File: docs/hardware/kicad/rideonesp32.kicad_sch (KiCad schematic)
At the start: 0 parts

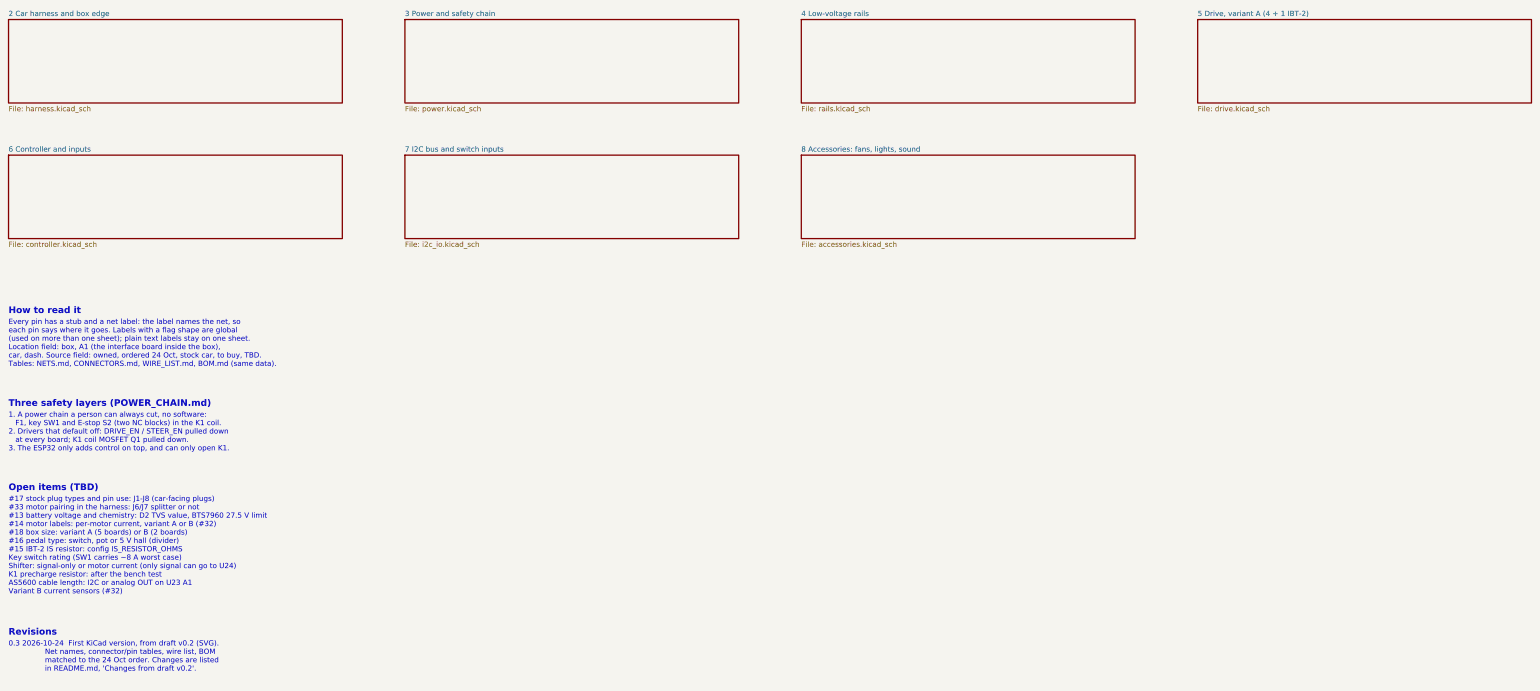
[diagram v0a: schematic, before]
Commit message: Schematic index: say what each sheet box holds and how to open it
The sheet symbols on page 1 were empty boxes, which read as missing
content. Each now carries a short summary of its sheet.

Co-Authored-By: Claude Opus 5.5 (1M context) <noreply@anthropic.com>
Claude-Session: https://claude.ai/code/session_01BSRw381bu7GTvawcDjL4S1
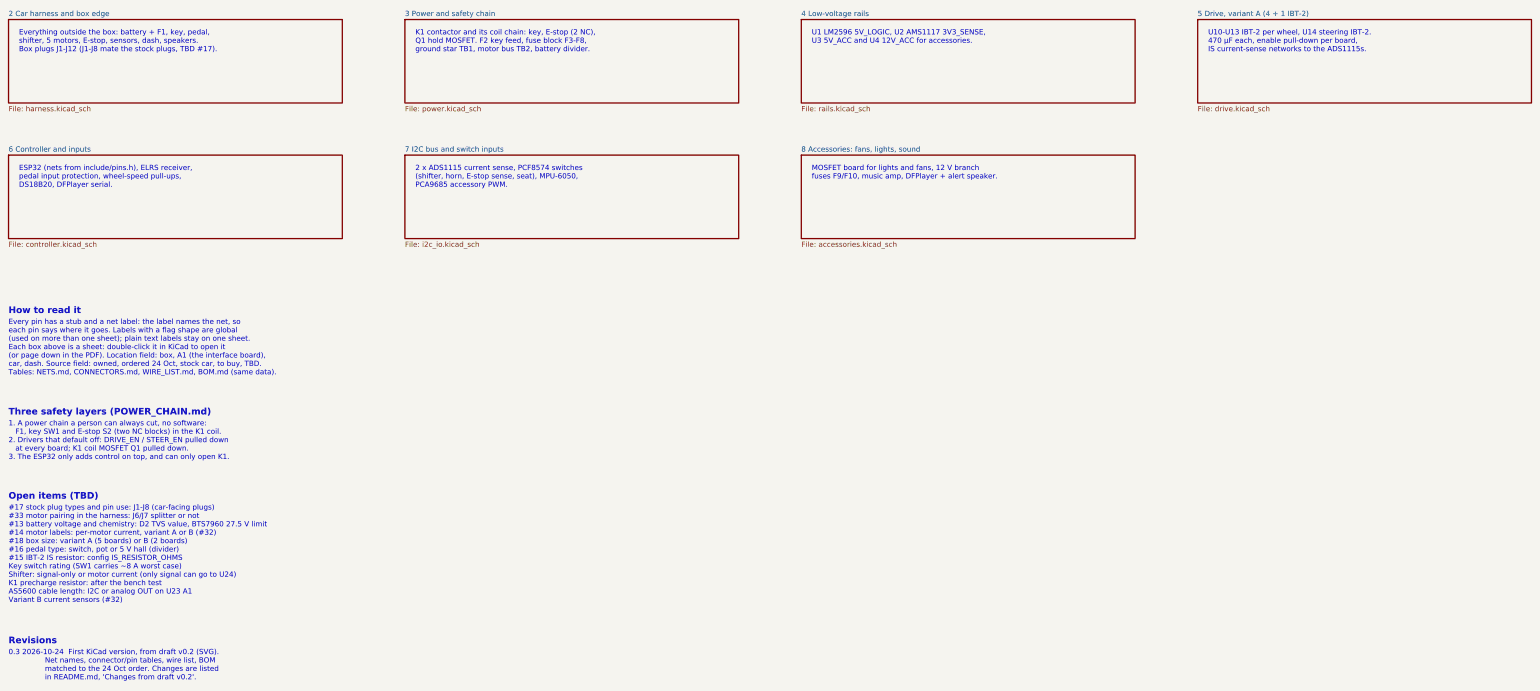
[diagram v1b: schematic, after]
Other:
- note added: "2 x ADS1115 current sense, PCF8574 switches (shifter, horn, E-stop sense, seat), MPU-6050, PCA9685 accessory PWM."
- note added: "ESP32 (nets from include/pins.h), ELRS receiver, pedal input protection, wheel-speed pull-ups, DS18B20, DFPlayer serial."
- note added: "Every pin has a stub and a net label: the label names the net, so each pin says where it goes. Labels with a flag shape are global (used on more than one sheet); plain text labels stay on one sheet. Each box above is a sheet: double-click it in KiCad to open it (or page down in the PDF). Location field: box, A1 (the interface board), car, dash. Source field: owned, ordered 24 Oct, stock car, to b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"
- note added: "Everything outside the box: battery + F1, key, pedal, shifter, 5 motors, E-stop, sensors, dash, speakers. Box plugs J1-J12 (J1-J8 mate the stock plugs, TBD #17)."
- note added: "K1 contactor and its coil chain: key, E-stop (2 NC), Q1 hold MOSFET. F2 key feed, fuse block F3-F8, ground star TB1, motor bus TB2, battery divider."
- note added: "MOSFET board for lights and fans, 12 V branch fuses F9/F10, music amp, DFPlayer + alert speaker."
- note added: "U1 LM2596 5V_LOGIC, U2 AMS1117 3V3_SENSE, U3 5V_ACC and U4 12V_ACC for accessories."
- note added: "U10-U13 IBT-2 per wheel, U14 steering IBT-2. 470 µF each, enable pull-down per board, IS current-sense networks to the ADS1115s."
- note removed: "Every pin has a stub and a net label: the label names the net, so each pin says where it goes. Labels with a flag shape are global (used on more than one sheet); plain text labels stay on one sheet. Location field: box, A1 (the interface board inside the box), car, dash. Source field: owned, ordered 24 Oct, stock car, to buy, TBD. Tables: NETS.md, CONNECTORS.md, WIRE_LIST.md, BOM.md (same data)."
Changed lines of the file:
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@@
   (instances (project "rideonesp32" (path "/e0e78d72-bf5c-51da-8e0f-d8642949b63b" (page "2"))))
 )
+(text "Everything outside the box: battery + F1, key, pedal,\nshifter, 5 motors, E-stop, sensors, dash, speakers.\nBox plugs J1-J12 (J1-J8 mate the stock plugs, TBD #17)." (exclude_from_sim no) (at 22.86 33.02 0) (effects (font (size 1.27 1.27)) (justify left top)))
 (sheet (at 116.84 30.48) (size 81.28 20.32) (exclude_from_sim no) (in_bom yes) (on_board yes) (dnp no)
   (stroke (width 0.1524) (type solid)) (fill (color 0 0 0 0.0000))
@@
   (instances (project "rideonesp32" (path "/e0e78d72-bf5c-51da-8e0f-d8642949b63b" (page "3"))))
 )
+(text "K1 contactor and its coil chain: key, E-stop (2 NC),\nQ1 hold MOSFET. F2 key feed, fuse block F3-F8,\nground star TB1, motor bus TB2, battery divider." (exclude_from_sim no) (at 119.38 33.02 0) (effects (font (size 1.27 1.27)) (justify left top)))
 (sheet (at 213.36 30.48) (size 81.28 20.32) (exclude_from_sim no) (in_bom yes) (on_board yes) (dnp no)
   (stroke (width 0.1524) (type solid)) (fill (color 0 0 0 0.0000))
@@
   (instances (project "rideonesp32" (path "/e0e78d72-bf5c-51da-8e0f-d8642949b63b" (page "4"))))
 )
+(text "U1 LM2596 5V_LOGIC, U2 AMS1117 3V3_SENSE,\nU3 5V_ACC and U4 12V_ACC for accessories." (exclude_from_sim no) (at 215.9 33.02 0) (effects (font (size 1.27 1.27)) (justify left top)))
 (sheet (at 309.88 30.48) (size 81.28 20.32) (exclude_from_sim no) (in_bom yes) (on_board yes) (dnp no)
   (stroke (width 0.1524) (type solid)) (fill (color 0 0 0 0.0000))
@@
   (instances (project "rideonesp32" (path "/e0e78d72-bf5c-51da-8e0f-d8642949b63b" (page "5"))))
 )
+(text "U10-U13 IBT-2 per wheel, U14 steering IBT-2.\n470 µF each, enable pull-down per board,\nIS current-sense networks to the ADS1115s." (exclude_from_sim no) (at 312.42 33.02 0) (effects (font (size 1.27 1.27)) (justify left top)))
 (sheet (at 20.32 63.5) (size 81.28 20.32) (exclude_from_sim no) (in_bom yes) (on_board yes) (dnp no)
   (stroke (width 0.1524) (type solid)) (fill (color 0 0 0 0.0000))
@@
   (instances (project "rideonesp32" (path "/e0e78d72-bf5c-51da-8e0f-d8642949b63b" (page "6"))))
 )
+(text "ESP32 (nets from include/pins.h), ELRS receiver,\npedal input protection, wheel-speed pull-ups,\nDS18B20, DFPlayer serial." (exclude_from_sim no) (at 22.86 66.04 0) (effects (font (size 1.27 1.27)) (justify left top)))
 (sheet (at 116.84 63.5) (size 81.28 20.32) (exclude_from_sim no) (in_bom yes) (on_board yes) (dnp no)
   (stroke (width 0.1524) (type solid)) (fill (color 0 0 0 0.0000))
@@
   (instances (project "rideonesp32" (path "/e0e78d72-bf5c-51da-8e0f-d8642949b63b" (page "7"))))
 )
+(text "2 x ADS1115 current sense, PCF8574 switches\n(shifter, horn, E-stop sense, seat), MPU-6050,\nPCA9685 accessory PWM." (exclude_from_sim no) (at 119.38 66.04 0) (effects (font (size 1.27 1.27)) (justify left top)))
 (sheet (at 213.36 63.5) (size 81.28 20.32) (exclude_from_sim no) (in_bom yes) (on_board yes) (dnp no)
   (stroke (width 0.1524) (type solid)) (fill (color 0 0 0 0.0000))
@@
   (instances (project "rideonesp32" (path "/e0e78d72-bf5c-51da-8e0f-d8642949b63b" (page "8"))))
 )
+(text "MOSFET board for lights and fans, 12 V branch\nfuses F9/F10, music amp, DFPlayer + alert speaker." (exclude_from_sim no) (at 215.9 66.04 0) (effects (font (size 1.27 1.27)) (justify left top)))
 (text "How to read it" (exclude_from_sim no) (at 20.32 100.52 0) (effects (font (size 1.6 1.6) (bold yes)) (justify left top)))
-(text "Every pin has a stub and a net label: the label names the net, so\neach pin says where it goes. Labels with a flag shape are global\n(used on more than one sheet); plain text labels stay on one sheet.\nLocation field: box, A1 (the interface board inside the box),\ncar, dash. Source field: owned, ordered 24 Oct, stock car, to buy, TBD.\nTables: NETS.md, CONNECTORS.md, WIRE_LIST.md, BOM.md (same data)." (exclude_from_sim no) (at 20.32 103.52 0) (effects (font (size 1.27 1.27)) (justify left top)))
-(text "Three safety layers (POWER_CHAIN.md)" (exclude_from_sim no) (at 20.32 123.12 0) (effects (font (size 1.6 1.6) (bold yes)) (justify left top)))
-(text "1. A power chain a person can always cut, no software:\n   F1, key SW1 and E-stop S2 (two NC blocks) in the K1 coil.\n2. Drivers that default off: DRIVE_EN / STEER_EN pulled down\n   at every board; K1 coil MOSFET Q1 pulled down.\n3. The ESP32 only adds control on top, and can only open K1." (exclude_from_sim no) (at 20.32 126.12 0) (effects (font (size 1.27 1.27)) (justify left top)))
-(text "Open items (TBD)" (exclude_from_sim no) (at 20.32 143.62 0) (effects (font (size 1.6 1.6) (bold yes)) (justify left top)))
-(text "#17 stock plug types and pin use: J1-J8 (car-facing plugs)\n#33 motor pairing in the harness: J6/J7 splitter or not\n#13 battery voltage and chemistry: D2 TVS value, BTS7960 27.5 V limit\n#14 motor labels: per-motor current, variant A or B (#32)\n#18 box size: variant A (5 boards) or B (2 boards)\n#16 pedal type: switch, pot or 5 V hall (divider)\n#15 IBT-2 IS resistor: config IS_RESISTOR_OHMS\nKey switch rating (SW1 carries ~8 A worst case)\nShifter: signal-only or motor current (only signal can go to U24)\nK1 precharge resistor: after the bench test\nAS5600 cable length: I2C or analog OUT on U23 A1\nVariant B current sensors (#32)" (exclude_from_sim no) (at 20.32 146.62 0) (effects (font (size 1.27 1.27)) (justify left top)))
-(text "Revisions" (exclude_from_sim no) (at 20.32 178.82 0) (effects (font (size 1.6 1.6) (bold yes)) (justify left top)))
-(text "0.3 2026-10-24  First KiCad version, from draft v0.2 (SVG).\n                Net names, connector/pin tables, wire list, BOM\n                matched to the 24 Oct order. Changes are listed\n                in README.md, 'Changes from draft v0.2'." (exclude_from_sim no) (at 20.32 181.82 0) (effects (font (size 1.27 1.27)) (justify left top)))
+(text "Every pin has a stub and a net label: the label names the net, so\neach pin says where it goes. Labels with a flag shape are global\n(used on more than one sheet); plain text labels stay on one sheet.\nEach box above is a sheet: double-click it in KiCad to open it\n(or page down in the PDF). Location field: box, A1 (the interface board),\ncar, dash. Source field: owned, ordered 24 Oct, stock car, to buy, TBD.\nTables: NETS.md, CONNECTORS.md, WIRE_LIST.md, BOM.md (same data)." (exclude_from_sim no) (at 20.32 103.52 0) (effects (font (size 1.27 1.27)) (justify left top)))
+(text "Three safety layers (POWER_CHAIN.md)" (exclude_from_sim no) (at 20.32 125.22 0) (effects (font (size 1.6 1.6) (bold yes)) (justify left top)))
+(text "1. A power chain a person can always cut, no software:\n   F1, key SW1 and E-stop S2 (two NC blocks) in the K1 coil.\n2. Drivers that default off: DRIVE_EN / STEER_EN pulled down\n   at every board; K1 coil MOSFET Q1 pulled down.\n3. The ESP32 only adds control on top, and can only open K1." (exclude_from_sim no) (at 20.32 128.22 0) (effects (font (size 1.27 1.27)) (justify left top)))
+(text "Open items (TBD)" (exclude_from_sim no) (at 20.32 145.72 0) (effects (font (size 1.6 1.6) (bold yes)) (justify left top)))
+(text "#17 stock plug types and pin use: J1-J8 (car-facing plugs)\n#33 motor pairing in the harness: J6/J7 splitter or not\n#13 battery voltage and chemistry: D2 TVS value, BTS7960 27.5 V limit\n#14 motor labels: per-motor current, variant A or B (#32)\n#18 box size: variant A (5 boards) or B (2 boards)\n#16 pedal type: switch, pot or 5 V hall (divider)\n#15 IBT-2 IS resistor: config IS_RESISTOR_OHMS\nKey switch rating (SW1 carries ~8 A worst case)\nShifter: signal-only or motor current (only signal can go to U24)\nK1 precharge resistor: after the bench test\nAS5600 cable length: I2C or analog OUT on U23 A1\nVariant B current sensors (#32)" (exclude_from_sim no) (at 20.32 148.72 0) (effects (font (size 1.27 1.27)) (justify left top)))
+(text "Revisions" (exclude_from_sim no) (at 20.32 180.92 0) (effects (font (size 1.6 1.6) (bold yes)) (justify left top)))
+(text "0.3 2026-10-24  First KiCad version, from draft v0.2 (SVG).\n                Net names, connector/pin tables, wire list, BOM\n                matched to the 24 Oct order. Changes are listed\n                in README.md, 'Changes from draft v0.2'." (exclude_from_sim no) (at 20.32 183.92 0) (effects (font (size 1.27 1.27)) (justify left top)))
 (sheet_instances (path "/" (page "1")))
 (embedded_fonts no)

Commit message: Schematic: add a system wiring overview page (every assembly joined on one A2 sheet)
Page 2 is a drawing-only overview generated by gen/overview.py; the net
sheets move to pages 3-9. ERC and the netlist check are unchanged.

Co-Authored-By: Claude Opus 5.5 (1M context) <noreply@anthropic.com>
Claude-Session: https://claude.ai/code/session_01BSRw381bu7GTvawcDjL4S1
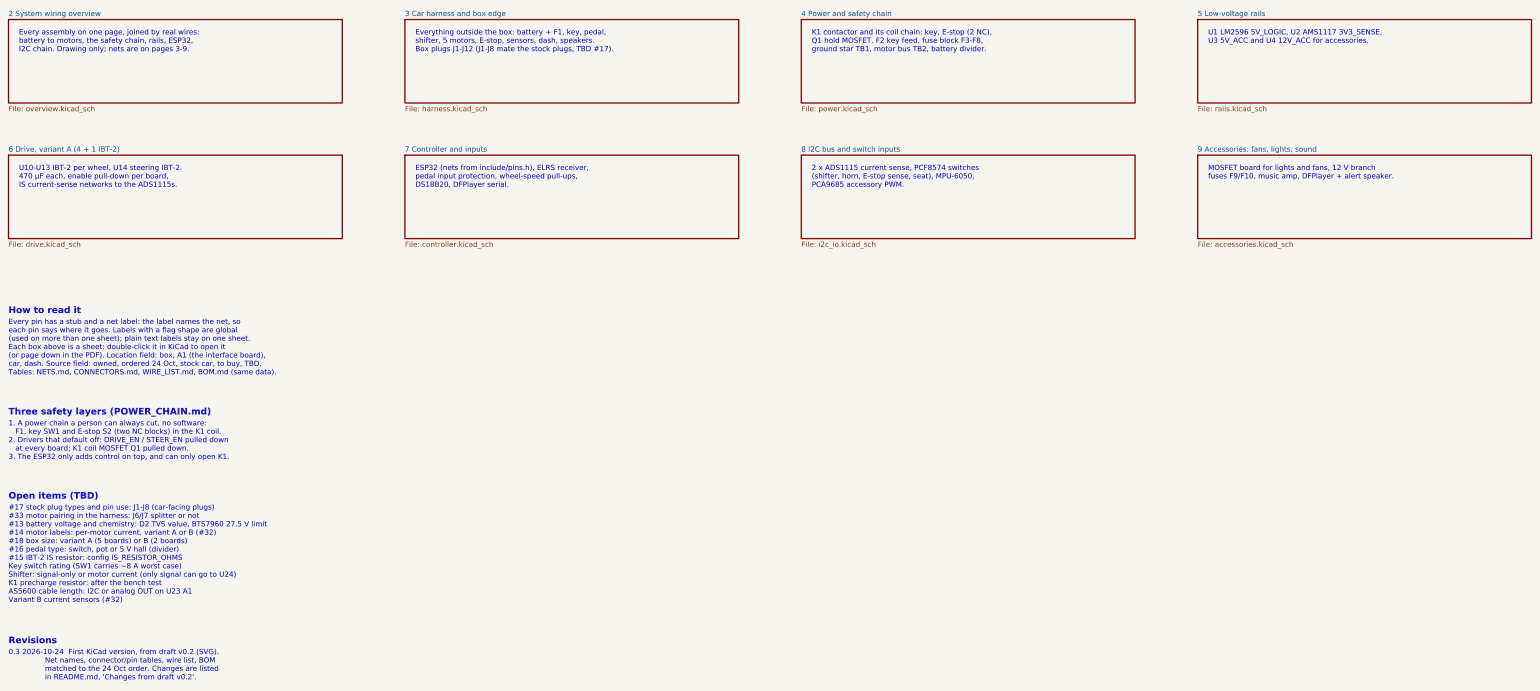
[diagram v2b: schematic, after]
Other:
- sheet 2 Car harness and box edge renamed 3 Car harness and box edge
- sheet 3 Power and safety chain renamed 4 Power and safety chain
- sheet 4 Low-voltage rails renamed 5 Low-voltage rails
- sheet 5 Drive, variant A (4 + 1 IBT-2) renamed 6 Drive, variant A (4 + 1 IBT-2)
- sheet 6 Controller and inputs renamed 7 Controller and inputs
- sheet 7 I2C bus and switch inputs renamed 8 I2C bus and switch inputs
- sheet 8 Accessories: fans, lights, sound renamed 9 Accessories: fans, lights, sound
- added sheet 2 System wiring overview (overview.kicad_sch)
- note added: "Every assembly on one page, joined by real wires: battery to motors, the safety chain, rails, ESP32, I2C chain. Drawing only; nets are on pages 3-9."

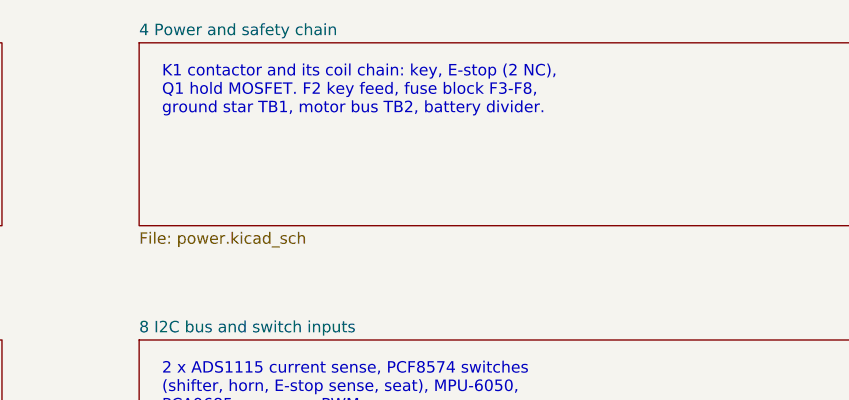
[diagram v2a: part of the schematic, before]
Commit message: Match the firmware to schematic v0.3: current scaling, contactor checks, fans
- Current sense divides by half the per-pin IS resistor (IS_PIN_RESISTOR_OHMS),
  since R_IS and L_IS are joined; it read about half the real current before.
  The DRIVER level now comes from the resistor (1.8 V with 1k boards).
- DRIVER and OVERCUR open the contactor: a shorted MOSFET ignores DRIVE_EN.
  The drive enable drops before the contactor opens.
- Motor-bus sense: R5-R7 in the schematic (150k/12k to ADS1115 #2 A2, 2.2k
  bleed). New ContactorCheck: K1 stays open at boot until the bus drains
  (K1_WELD if it doesn't, permanent), and NO_BUS when K1 is held closed with
  no bus.
- I2C at 100 kHz, the PCF8574's rating.
- Box fans full on through PCA9685 channel 1; DS18B20 read with our own
  1-Wire timing; new HOT fault (65 C, hysteresis to 55 C).
- WHEEL_REVERSED per wheel in config.h.

Co-Authored-By: Claude Opus 5.5 (1M context) <noreply@anthropic.com>
Claude-Session: https://claude.ai/code/session_01BrgYX7MqpwRKNfNAgoiyH8
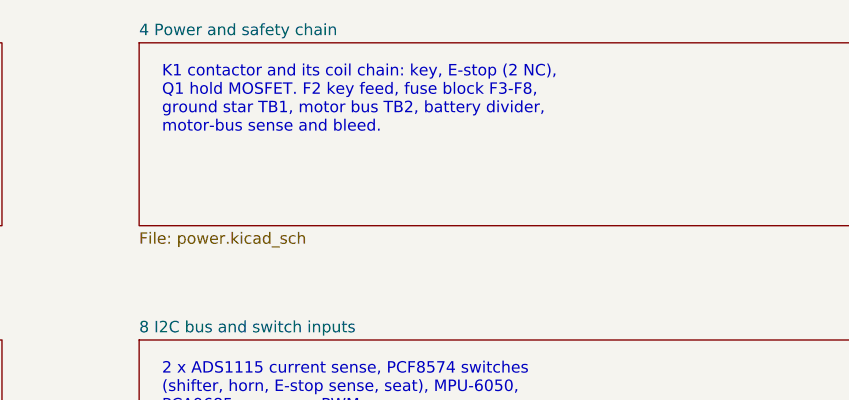
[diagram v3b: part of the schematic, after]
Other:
- note added: "K1 contactor and its coil chain: key, E-stop (2 NC), Q1 hold MOSFET. F2 key feed, fuse block F3-F8, ground star TB1, motor bus TB2, battery divider, motor-bus sense and bleed."
- note removed: "K1 contactor and its coil chain: key, E-stop (2 NC), Q1 hold MOSFET. F2 key feed, fuse block F3-F8, ground star TB1, motor bus TB2, battery divider."
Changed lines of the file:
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@@
   (instances (project "rideonesp32" (path "/e0e78d72-bf5c-51da-8e0f-d8642949b63b" (page "4"))))
 )
-(text "K1 contactor and its coil chain: key, E-stop (2 NC),\nQ1 hold MOSFET. F2 key feed, fuse block F3-F8,\nground star TB1, motor bus TB2, battery divider." (exclude_from_sim no) (at 215.9 33.02 0) (effects (font (size 1.27 1.27)) (justify left top)))
+(text "K1 contactor and its coil chain: key, E-stop (2 NC),\nQ1 hold MOSFET. F2 key feed, fuse block F3-F8,\nground star TB1, motor bus TB2, battery divider,\nmotor-bus sense and bleed." (exclude_from_sim no) (at 215.9 33.02 0) (effects (font (size 1.27 1.27)) (justify left top)))
 (sheet (at 309.88 30.48) (size 81.28 20.32) (exclude_from_sim no) (in_bom yes) (on_board yes) (dnp no)
   (stroke (width 0.1524) (type solid)) (fill (color 0 0 0 0.0000))
